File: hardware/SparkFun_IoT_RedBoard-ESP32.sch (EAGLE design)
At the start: 121 parts, among them J1 5.5x2.1mm Barrel, J13 QWIIC_RIGHT_ANGLE, J15 MICRO-SD-PUSH-PUSH-EXT-PIN, J2 USB-C, J3 USB_SOLDER_PADS, J5 M10NO_SILK, Q1 MBT3904DW1T1, Q11 20V/4.2A/52mΩ/1.4W, Q13 20V/4.2A/52mΩ/1.4W, Q3 20V/4.2A/52mΩ/1.4W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

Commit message: Design review updates
Clean up SHLD jumper in schematic
Clean up boot mode table
Doot
Move C8 closer to CH340
Fix natural bridges
Improve GND continuity
Add 10uF cap to uSD
Switch 3V regulator
Replace LED footprints with non-hidden silk
Add NO jumper between RGB LED DO and NC pin
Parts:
- added C19: 10uF, SparkFun-Capacitors:10UF-0603-6.3V-20%
- added JP10: LED_DO, SparkFun-Jumpers:JUMPER-SMT_2_NO_SILK
- D2: device SparkFun-LED:LED-GREEN_HIDDENSILK -> SparkFun-LED:LED-GREEN1206
- D3, D4: value YELLOW -> Yellow; device SparkFun-LED:LED-YELLOW_HIDDENSILK -> SparkFun-LED:LED-YELLOWLILYPAD
- D5: value GREEN -> RED; device SparkFun-LED:LED-RED_HIDDENSILK -> SparkFun-LED:LED-RED1206
- D6: device SparkFun-LED:LED-BLUE_HIDDENSILK -> SparkFun-LED:LED-BLUE1206
- U4: value 3.3V -> XC6222B331MR-G; device SparkFun-IC-Power:V_REG_AP2112K-3.3V -> SparkFun-IC-Power:XC6222B331MR-G
- renumbered S2 to DOOT
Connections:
- new net LED_DO: J10.1, J9.1, JP10.2
- new net N$35: D7.DO, JP10.1
- net 3.3V: now also C19.1
- net ESP32_GPIO12_TDI: now also U1.POCI2/IOA12; no longer U1.MISO2/IOA12
- net ESP32_GPIO13_TCK: now also U1.PICO2/IOA13; no longer U1.MOSI2/IOA13
- net ESP32_GPIO19_POCI: now also U1.POCI3/IO19; no longer U1.MISO3/IO19
- net ESP32_GPIO23_PICO: now also U1.PICO3/IO23; no longer U1.MOSI3/IO23
- net GND: now also C19.2
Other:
- note added: "0"
- note added: "1"
- note added: "Boot Mode Configuration"
- note added: "Bootloader"
- note added: "Default"
- note added: "IO0"
- note added: "IO12"
- note added: "IO12 = MDTI, IO15 = MDTO"
- note added: "IO15"
- note added: "IO2"
- note added: "IO5"
- note added: "Pin"
- note added: "Run"
- note added: "x"
- note removed: "Boot Mode Configuration Pin Default Boot Download GPIO0 1 1 0 U0TXD 1 1 x GPIO2 0 x 0 GPIO4 0 x x MTDO 1 x x GPIO5 1 1 x If U0TXD, GPIO2, GPIO5 are floating, GPIO0 determines boot mode"
- moved on the sheet: C14, C5, R2, R3, SHLD

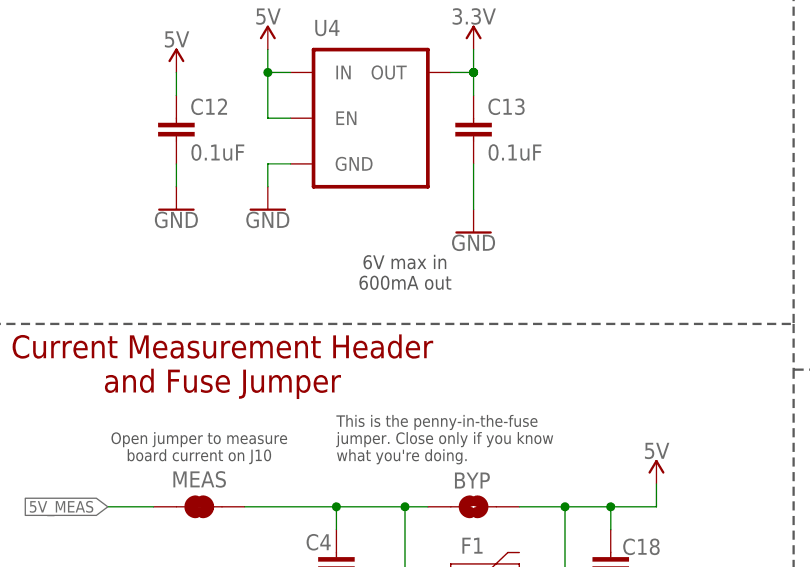
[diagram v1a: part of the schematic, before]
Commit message: Pre-production updates
Update regulator current in schematic
Change "LED DO" silk label to "NC/LED DO"
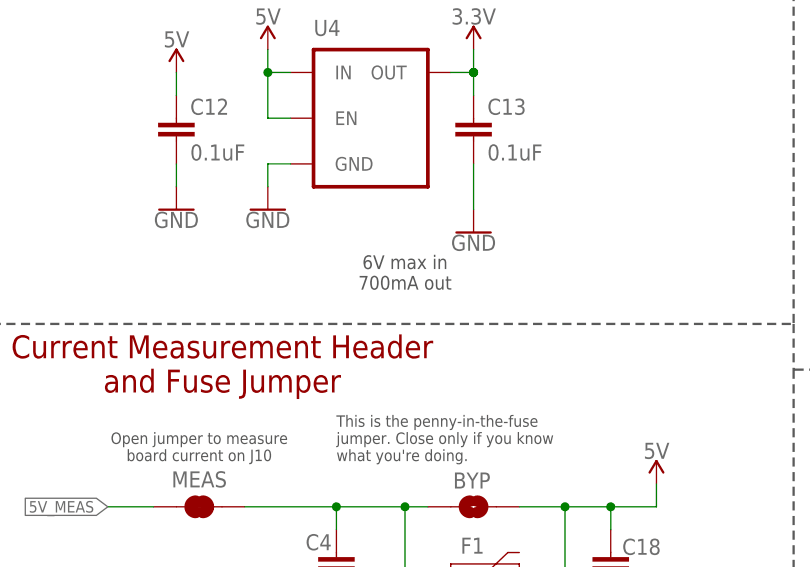
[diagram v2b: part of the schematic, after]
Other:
- note added: "6V max in 700mA out"
- note removed: "6V max in 600mA out"
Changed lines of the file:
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@@
 <text x="116.84" y="114.3" size="1.778" layer="97" font="vector">VIN Range: 7-15V</text>
 <text x="152.4" y="48.26" size="1.524" layer="97" font="vector" align="top-center">6V max in
-600mA out
+700mA out
 </text>
 <text x="309.88" y="157.48" size="2.032" layer="97" font="vector" rot="MR0" align="center-left">Charge current:

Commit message: Fix PROD_ID of new regulator
Didn't update when it was replaced for some reason
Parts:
- U4: PROD_ID VREG-12457 -> (none)
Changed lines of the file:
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@@
 <part name="SUPPLY18" library="SparkFun-PowerSymbols" deviceset="V_BATT" device=""/>
 <part name="C13" library="SparkFun-Capacitors" deviceset="0.1UF" device="-0603-25V-(+80/-20%)" value="0.1uF"/>
-<part name="U4" library="SparkFun-IC-Power" deviceset="XC6222" device="B331MR-G" value="XC6222B331MR-G">
-<attribute name="PROD_ID" value="VREG-12457"/>
-</part>
+<part name="U4" library="SparkFun-IC-Power" deviceset="XC6222" device="B331MR-G" value="XC6222B331MR-G"/>
 <part name="SUPPLY7" library="SparkFun-PowerSymbols" deviceset="3.3V" device=""/>
 <part name="SUPPLY21" library="SparkFun-PowerSymbols" deviceset="5V" device=""/>
